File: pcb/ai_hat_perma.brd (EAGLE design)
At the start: 65 x 56 mm, 285 parts, among them J1 1X01-SM, J10 1X01-SM, J100 1X01-SM, J101 1X01-SM, J102 1X01-SM, J103 1X01-SM, J104 1X01-SM, J105 1X01-SM, J106 1X01-SM, J107 1X01-SM, J108 1X01-SM, J109 1X01-SM, J11 1X01-SM, J110 1X01-SM, J111 1X01-SM, J112 1X01-SM, J113 1X01-SM, J114 1X01-SM, J115 1X01-SM, J116 1X01-SM, J117 1X01-SM, J118 1X01-SM, J119 1X01-SM, J12 1X01-SM, J120 1X01-SM, J121 1X01-SM, J122 1X01-SM, J123 1X01-SM, J124 1X01-SM, J125 1X01-SM, J126 1X01-SM, J127 1X01-SM, J128 1X01-SM, J129 1X01-SM, J13 1X01-SM, J130 1X01-SM, J131 1X01-SM, J132 1X01-SM, J133 1X01-SM, J134 1X01-SM, J135 1X01-SM, J136 1X01-SM, J137 1X01-SM, J138 1X01-SM, J139 1X01-SM, J14 1X01-SM, J140 1X01-SM, J141 1X01-SM, J142 1X01-SM, J143 1X01-SM, J144 1X01-SM, J145 1X01-SM, J146 1X01-SM, J147 1X01-SM, J148 1X01-SM, J149 1X01-SM, J15 1X01-SM, J150 1X01-SM, J151 1X01-SM, J152 1X01-SM, J153 1X01-SM, J154 1X01-SM, J155 1X01-SM, J156 1X01-SM, J157 1X01-SM, J158 1X01-SM, J159 1X01-SM, J16 1X01-SM, J160 1X01-SM, J161 1X01-SM, J162 1X01-SM, J163 1X01-SM, J164 1X01-SM, J165 1X01-SM, J166 1X01-SM, J167 1X01-SM, J168 1X01-SM, J169 1X01-SM, J17 1X01-SM, J170 1X01-SM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

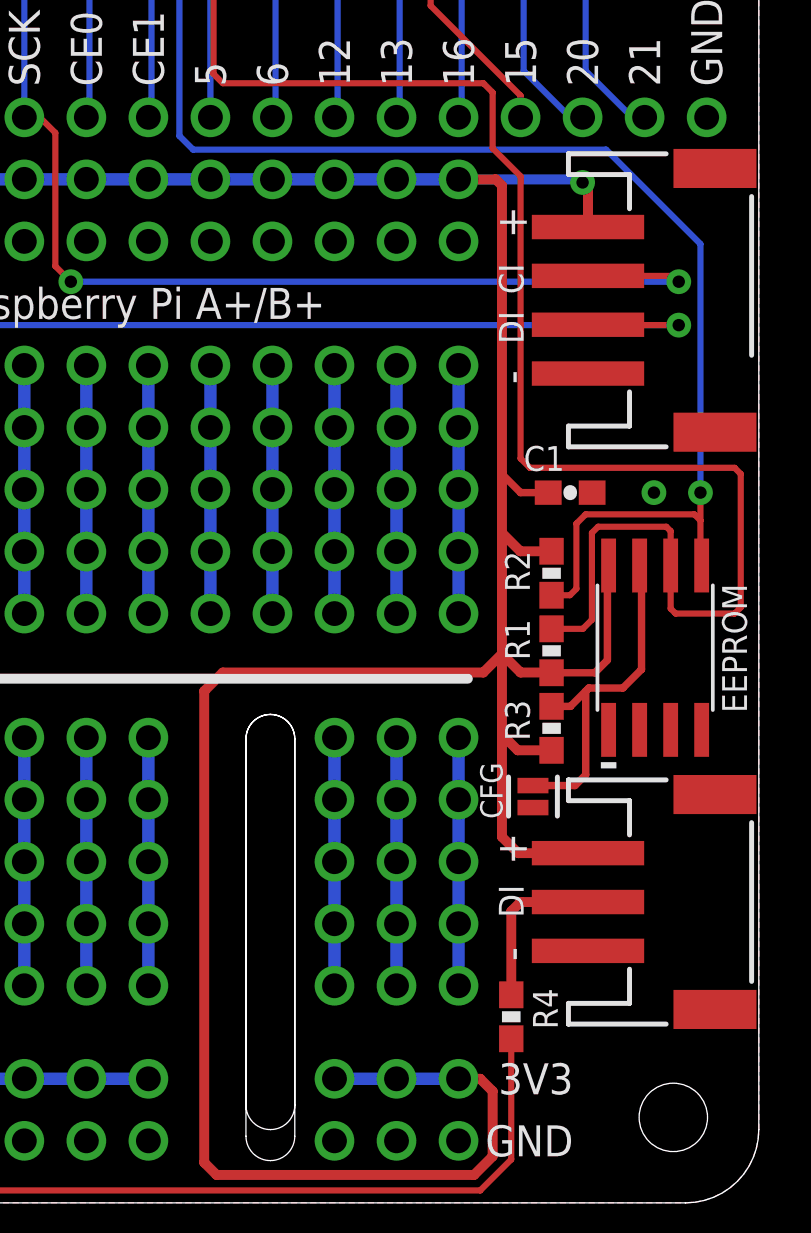
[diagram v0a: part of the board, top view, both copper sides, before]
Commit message: updating supply to LEDs
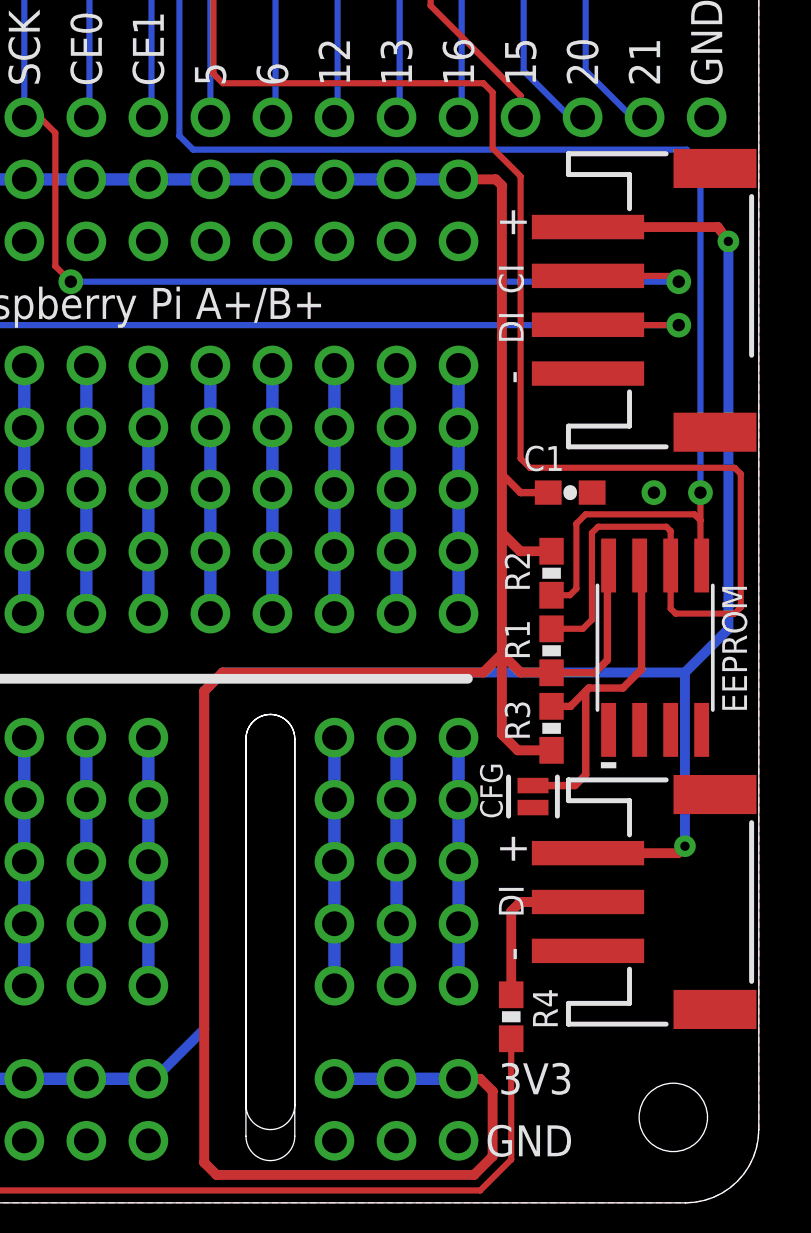
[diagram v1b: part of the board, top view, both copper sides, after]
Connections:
- net 3V3: no longer J18.1, J19.1
- net 5V: now also J18.1, J19.1
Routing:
- net 5V: track 86.2 -> 158.7 mm, vias 0 -> 2
- net 3V3: track 186.3 -> 171.3 mm, vias 1 -> 0
- net ID_SD: track 53.1 -> 55.0 mm
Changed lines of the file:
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@@
 <wire x1="7.669" y1="53.77" x2="6.985" y2="53.086" width="0.4064" layer="16"/>
 <wire x1="6.985" y1="53.086" x2="6.985" y2="48.26" width="0.4064" layer="16"/>
+<contactref element="J19" pad="1"/>
+<contactref element="J18" pad="1"/>
+<wire x1="58.006" y1="14.319" x2="61.69" y2="14.319" width="0.4064" layer="1"/>
+<wire x1="61.69" y1="14.319" x2="61.976" y2="14.605" width="0.4064" layer="1"/>
+<via x="61.976" y="14.605" extent="1-16" drill="0.381"/>
+<wire x1="61.976" y1="14.605" x2="61.976" y2="21.717" width="0.4064" layer="16"/>
+<wire x1="58.006" y1="39.957" x2="63.325" y2="39.957" width="0.4064" layer="1"/>
+<wire x1="63.325" y1="39.957" x2="63.754" y2="39.37" width="0.4064" layer="1"/>
+<via x="63.754" y="39.37" extent="1-16" drill="0.381"/>
+<wire x1="63.754" y1="39.37" x2="63.754" y2="23.495" width="0.4064" layer="16"/>
+<wire x1="40.132" y1="4.953" x2="42.291" y2="7.112" width="0.4064" layer="16"/>
+<wire x1="42.291" y1="7.112" x2="42.291" y2="20.955" width="0.4064" layer="16"/>
+<wire x1="42.291" y1="20.955" x2="43.053" y2="21.717" width="0.4064" layer="16"/>
+<wire x1="43.053" y1="21.717" x2="61.976" y2="21.717" width="0.4064" layer="16"/>
+<wire x1="61.976" y1="21.717" x2="63.754" y2="23.495" width="0.4064" layer="16"/>
 </signal>
 <signal name="3V3">
@@
 <wire x1="43.053" y1="21.717" x2="53.721" y2="21.717" width="0.4064" layer="1"/>
 <wire x1="53.721" y1="21.717" x2="54.483" y2="22.479" width="0.4064" layer="1"/>
-<contactref element="J19" pad="1"/>
-<contactref element="J18" pad="1"/>
-<wire x1="58.006" y1="14.319" x2="55.15" y2="14.319" width="0.4064" layer="1"/>
-<wire x1="55.15" y1="14.319" x2="54.483" y2="14.986" width="0.4064" layer="1"/>
-<wire x1="54.483" y1="14.986" x2="54.483" y2="19.177" width="0.4064" layer="1"/>
-<wire x1="58.006" y1="39.957" x2="58.006" y2="41.562" width="0.4064" layer="1"/>
-<wire x1="58.006" y1="41.562" x2="57.785" y2="41.783" width="0.4064" layer="1"/>
-<via x="57.785" y="41.783" extent="1-16" drill="0.508"/>
-<wire x1="57.785" y1="41.783" x2="57.658" y2="41.91" width="0.4064" layer="16"/>
-<wire x1="57.658" y1="41.91" x2="52.705" y2="41.91" width="0.4064" layer="16"/>
 <wire x1="8.37" y1="51.23" x2="8.37" y2="49.264" width="0.3048" layer="1"/>
 <wire x1="8.37" y1="49.264" x2="7.874" y2="48.768" width="0.3048" layer="1"/>
@@
 <wire x1="62.611" y1="27.94" x2="62.611" y2="29.083" width="0.254" layer="1"/>
 <via x="62.611" y="29.083" extent="1-16" drill="0.508"/>
-<wire x1="62.611" y1="29.083" x2="62.611" y2="39.264790625" width="0.254" layer="16"/>
+<wire x1="62.611" y1="29.083" x2="62.611" y2="42.566790625" width="0.254" layer="16"/>
 <wire x1="41.275" y1="43.688" x2="41.83560625" y2="43.12739375" width="0.254" layer="16"/>
-<wire x1="58.748396875" y1="43.12739375" x2="41.83560625" y2="43.12739375" width="0.254" layer="16"/>
-<wire x1="62.611" y1="39.264790625" x2="58.748396875" y2="43.12739375" width="0.254" layer="16"/>
+<wire x1="62.050396875" y1="43.12739375" x2="41.83560625" y2="43.12739375" width="0.254" layer="16"/>
+<wire x1="62.611" y1="42.566790625" x2="62.050396875" y2="43.12739375" width="0.254" layer="16"/>
 <wire x1="41.275" y1="51.115" x2="41.275" y2="43.688" width="0.254" layer="16"/>
 <wire x1="41.275" y1="51.115" x2="41.39" y2="51.23" width="0.254" layer="16"/>
